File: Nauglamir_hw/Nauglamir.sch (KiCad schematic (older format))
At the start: 70 parts, among them Q1 2N7002

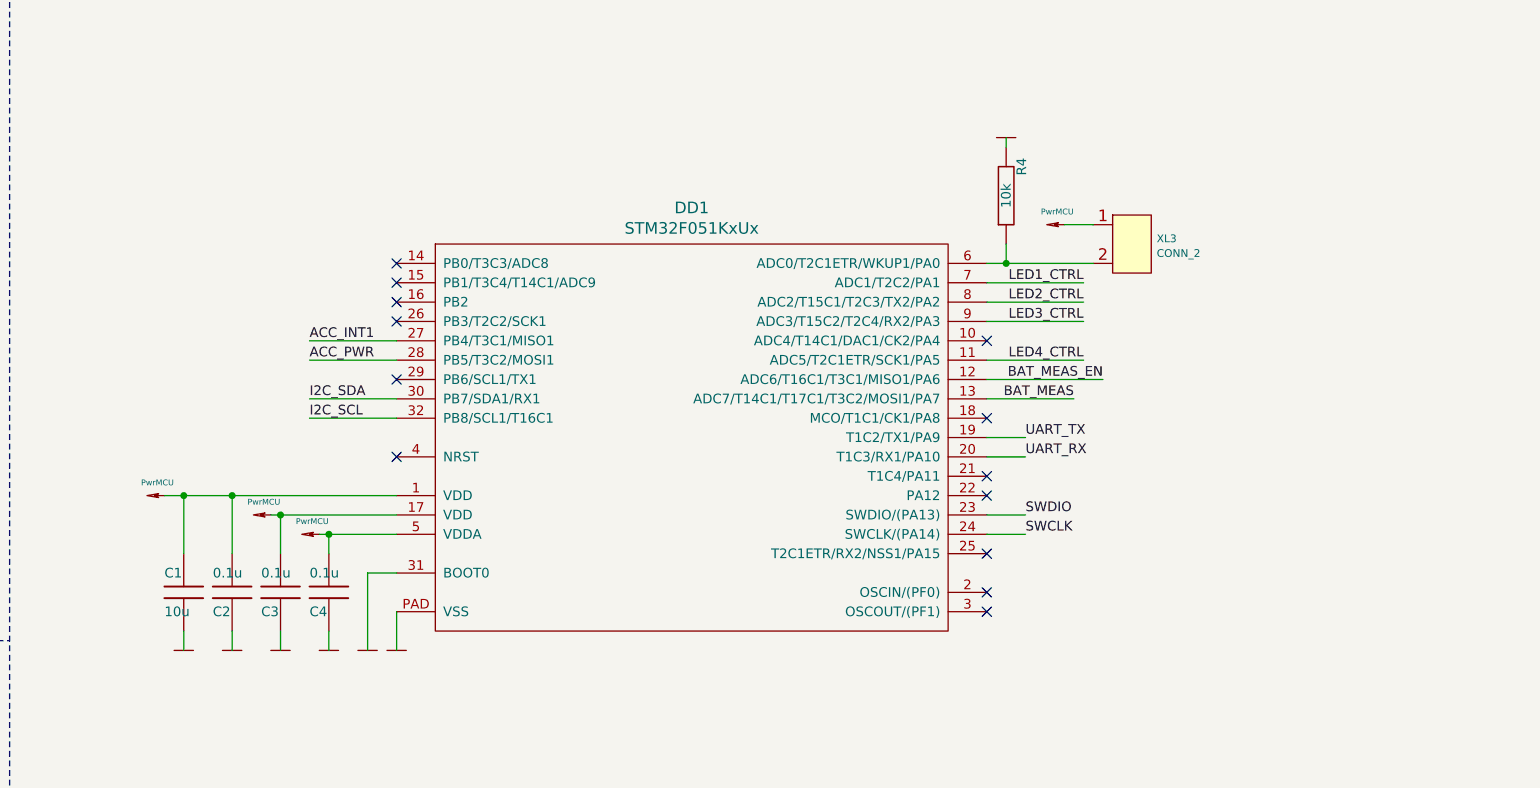
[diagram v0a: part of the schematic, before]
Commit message: PCB seems routed
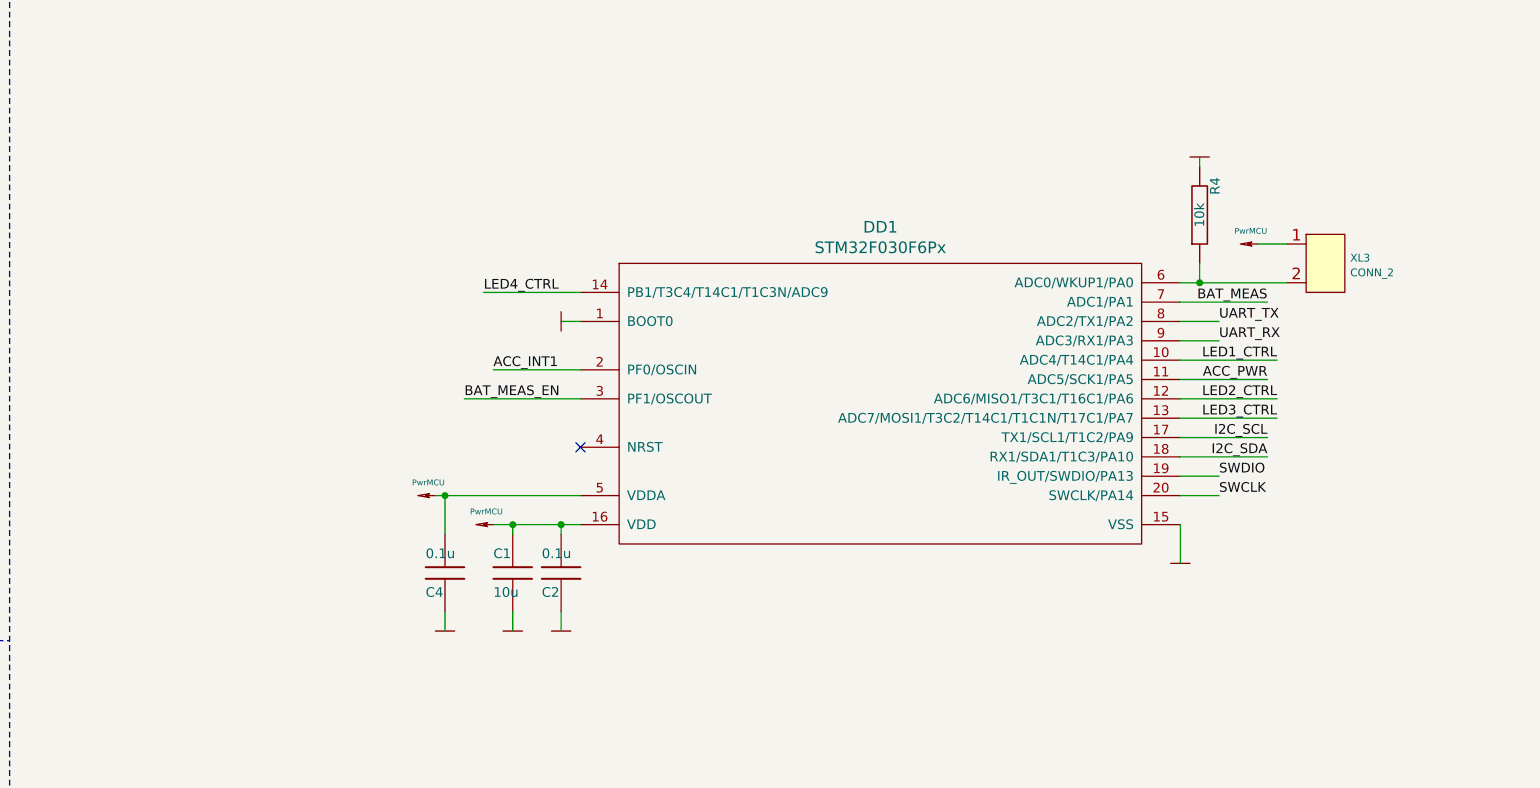
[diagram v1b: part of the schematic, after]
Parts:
- removed C3: 0.1u, Capacitors:CAP_0603_Silks, symbol Tittar_kl:C
- removed DD1: STM32F051KxUx, QFN_DFN:QFN-32_EP_5x5_Pitch0.5mm, symbol st_kl:STM32F051KxUx
- added DD1: STM32F030F6Px, SO_DIL_TSSOP:TSSOP20, symbol st_kl:STM32F030F6Px
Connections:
- net ACC_INT1: now also DD1.2 (PF0/OSCIN)
- net ACC_PWR: now also DD1.11 (ADC5/SCK1/PA5)
- net BAT_MEAS: now also DD1.7 (ADC1/PA1)
- net BAT_MEAS_EN: now also DD1.3 (PF1/OSCOUT)
- net GND: now also DD1.1 (BOOT0), DD1.15 (VSS)
- net I2C_SCL: now also DD1.17 (TX1/SCL1/T1C2/PA9)
- net I2C_SDA: now also DD1.18 (RX1/SDA1/T1C3/PA10)
- net LED1_CTRL: now also DD1.10 (ADC4/T14C1/PA4)
- net LED2_CTRL: now also DD1.12 (ADC6/MISO1/T3C1/T16C1/PA6)
- net LED3_CTRL: now also DD1.13 (ADC7/MOSI1/T3C2/T14C1/T1C1N/T17C1/PA7)
- net LED4_CTRL: now also DD1.14 (PB1/T3C4/T14C1/T1C3N/ADC9)
- net PwrMCU: now also DD1.16 (VDD), DD1.5 (VDDA)
- net SWCLK: now also DD1.20 (SWCLK/PA14)
- net SWDIO: now also DD1.19 (IR_OUT/SWDIO/PA13)
- net UART_RX: now also DD1.9 (ADC3/RX1/PA3)
- net UART_TX: now also DD1.8 (ADC2/TX1/PA2)
- net at R4.1, XL3.2 (PM): now also DD1.6 (ADC0/WKUP1/PA0)
- no-connect marks 14 -> 2
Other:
- moved on the sheet: C1, C2, C4, R4, XL3
